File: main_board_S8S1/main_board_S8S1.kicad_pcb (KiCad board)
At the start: 2 copper layers, 114.3 x 86.4 mm, 47 parts

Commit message: Обновлены футпринты светодиодов
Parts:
- HL3, HL4, HL5, HL6, HL7: footprint KCL:D0805 -> KCL:LED-SMD-0805

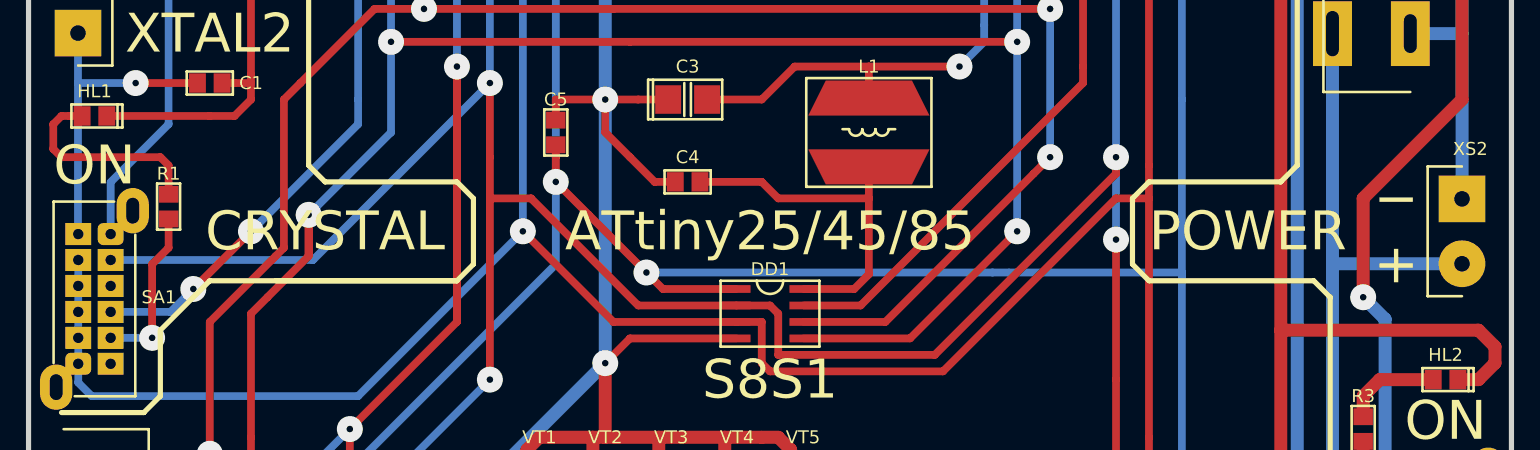
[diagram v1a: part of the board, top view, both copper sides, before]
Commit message: Обновлены футпринты светодиодов HL1, HL2
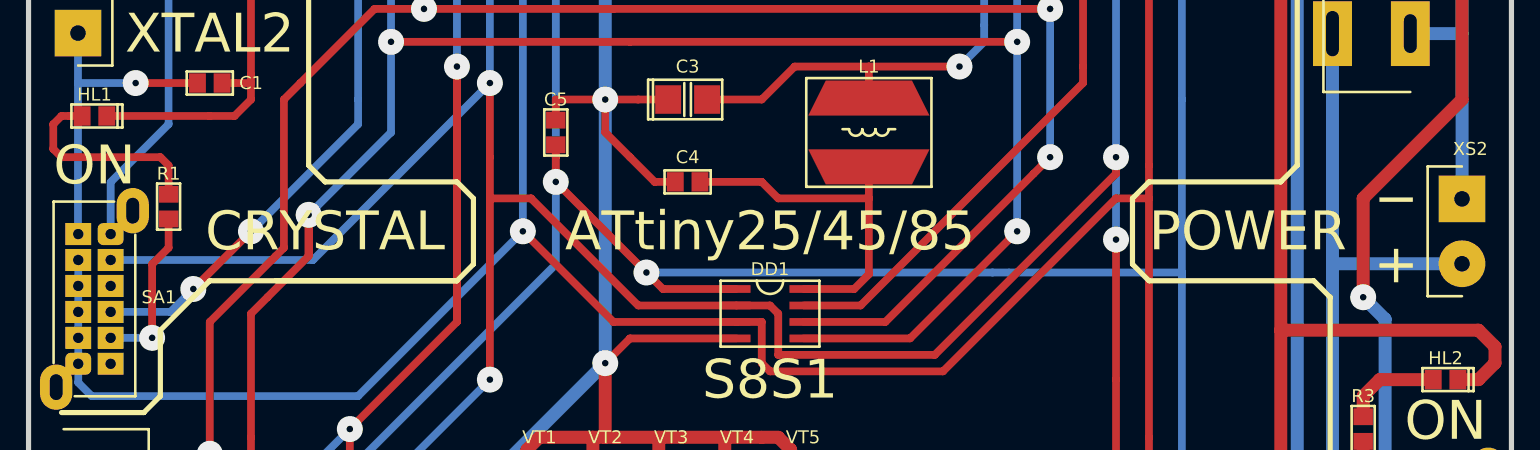
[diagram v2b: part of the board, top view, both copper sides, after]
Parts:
- HL1, HL2: footprint KCL:D0805 -> KCL:LED-SMD-0805

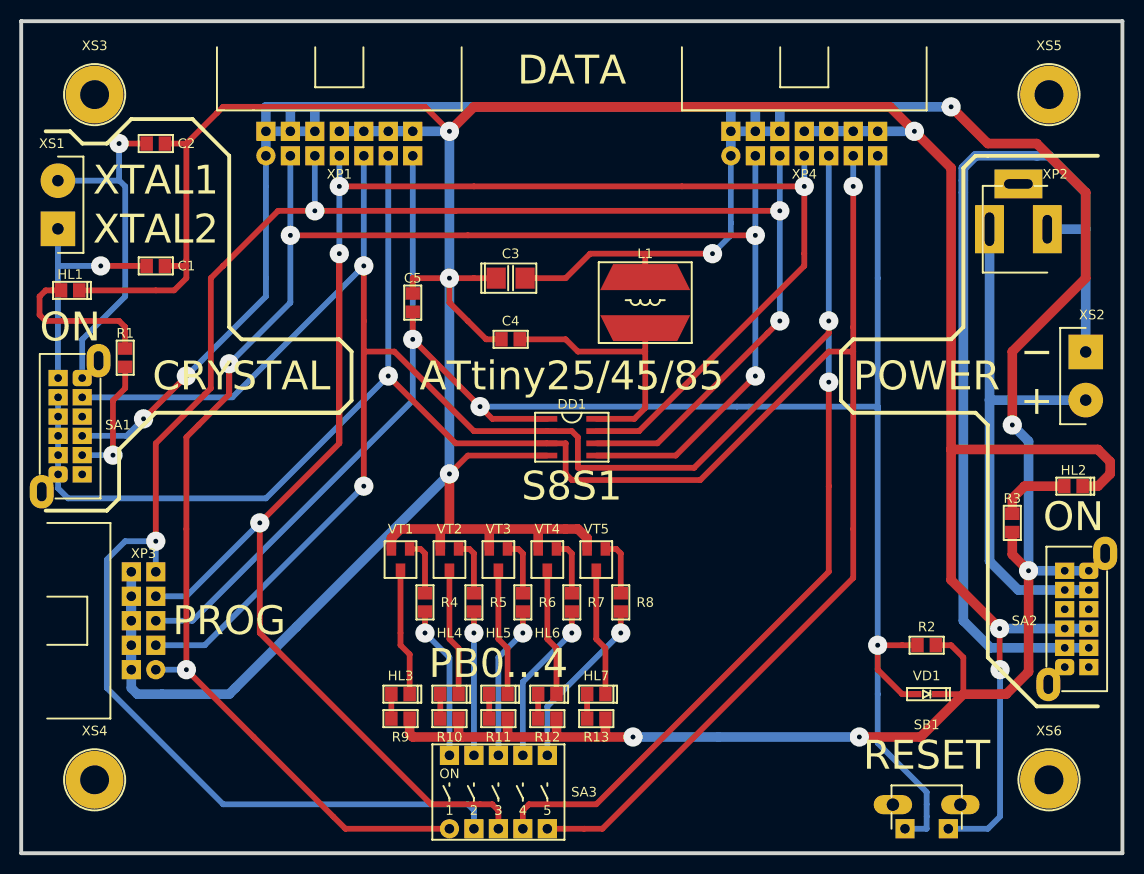
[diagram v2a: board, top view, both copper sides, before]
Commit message: Доработаны трассы, а также линии на слое F.SilkS (разделённые линии заменены цельными)
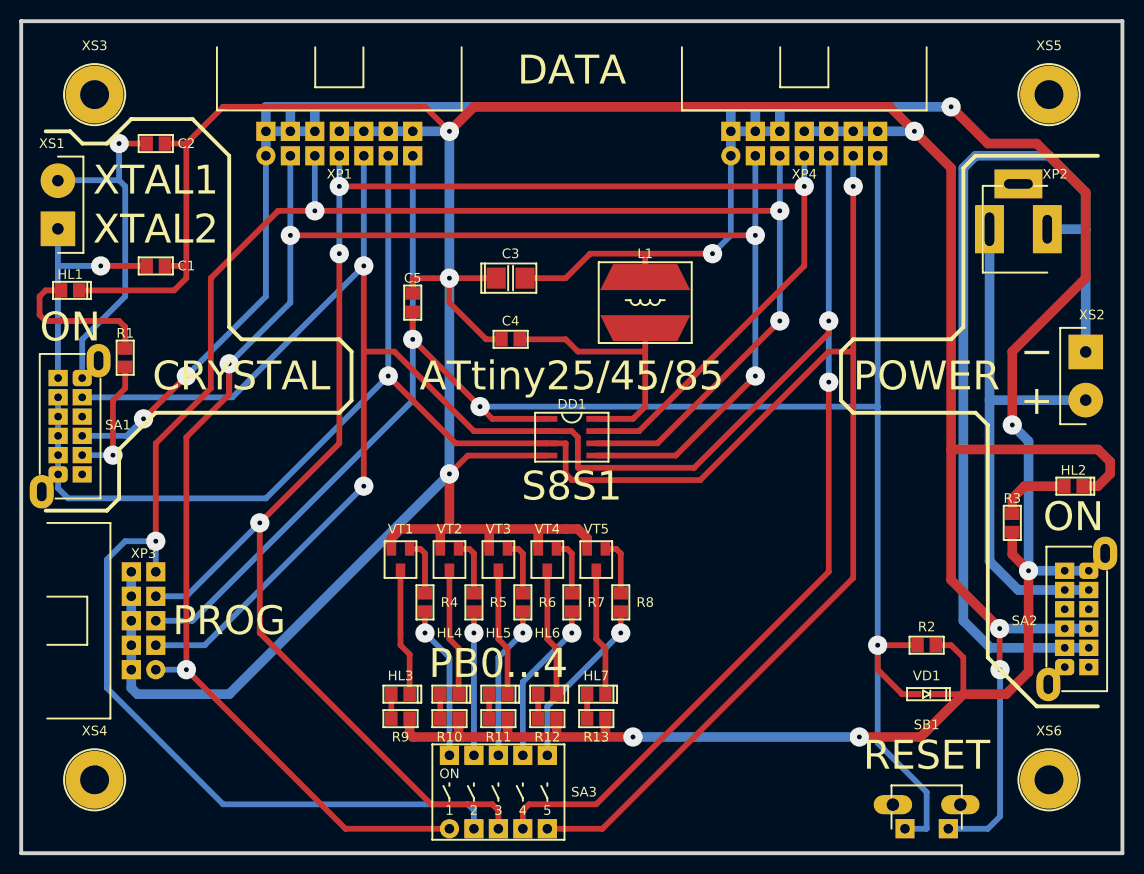
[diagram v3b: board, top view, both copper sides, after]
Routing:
- net GND: track 424.0 -> 401.2 mm
- net /PB2: track 209.2 -> 189.5 mm
- net /PB5: track 209.4 -> 208.8 mm

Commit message: В связи с доработкой библиотеки обновлено большинство футпринтов
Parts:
- C1, C2, C4, C5: footprint KCL:C0805 -> KCL:C-SMD-0805
- C3: footprint KCL:T3528 -> KCL:CP-SMD-3528
- DD1: footprint KCL:SO-08 -> KCL:P-SO-08
- L1: footprint KCL:SDR0805 -> KCL:L-SDR0805
- R1, R10, R11, R12, R13, R2, R3, R4, R5, R6, R7, R8, R9: footprint KCL:R0805 -> KCL:R-SMD-0805
- SA1, SA2: footprint KCL:SK-42D01-G -> KCL:SW-SK-42D01-G
- SA3: footprint KCL:NDI(R)-05 -> KCL:SW-NDI(R)-05
- SB1: footprint KCL:07125 -> KCL:SW-07125
- VD1: footprint KCL:SOD-323 -> KCL:P-SOD-323
- VT1, VT2, VT3, VT4, VT5: footprint KCL:SOT-23 -> KCL:P-SOT-23
- XP1, XP4: footprint KCL:IDC-14MR -> KCL:CON-IDC-14MR
- XP2: footprint KCL:PJ-002B -> KCL:CON-PJ-002B
- XP3: footprint KCL:IDC-10MR -> KCL:CON-IDC-10MR
- XS1, XS2: footprint KCL:DG301R-5.0-02P -> KCL:CON-DG301R-5.0-02P
- XS3, XS4, XS5, XS6: footprint KCL:DA5 -> KCL:STA-DA5
